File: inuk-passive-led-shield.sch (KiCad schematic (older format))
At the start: 12 parts, among them J1 Conn_01x04_Male, J2 Conn_01x10_Male, J3 Conn_01x02_Male

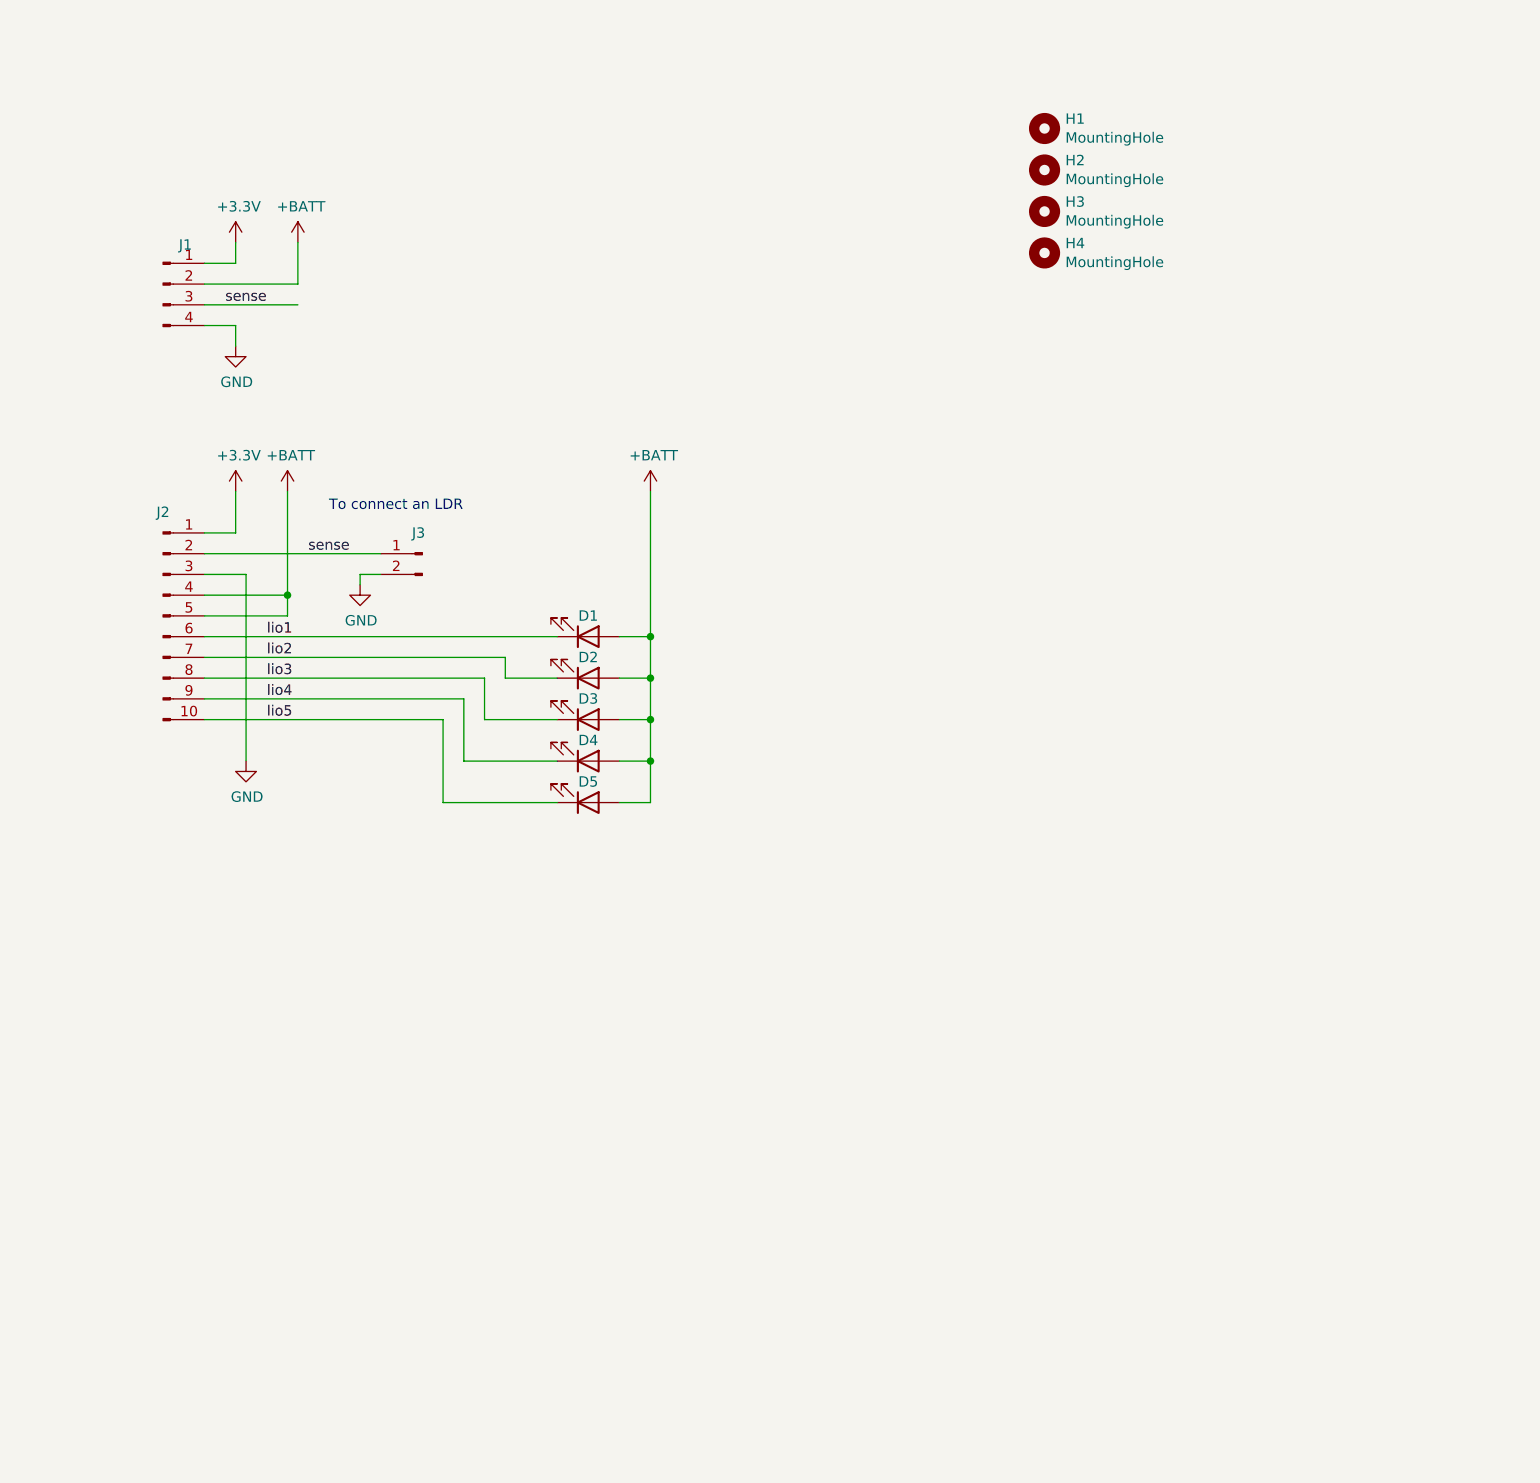
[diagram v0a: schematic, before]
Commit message: added logo and info text for rev 0.9
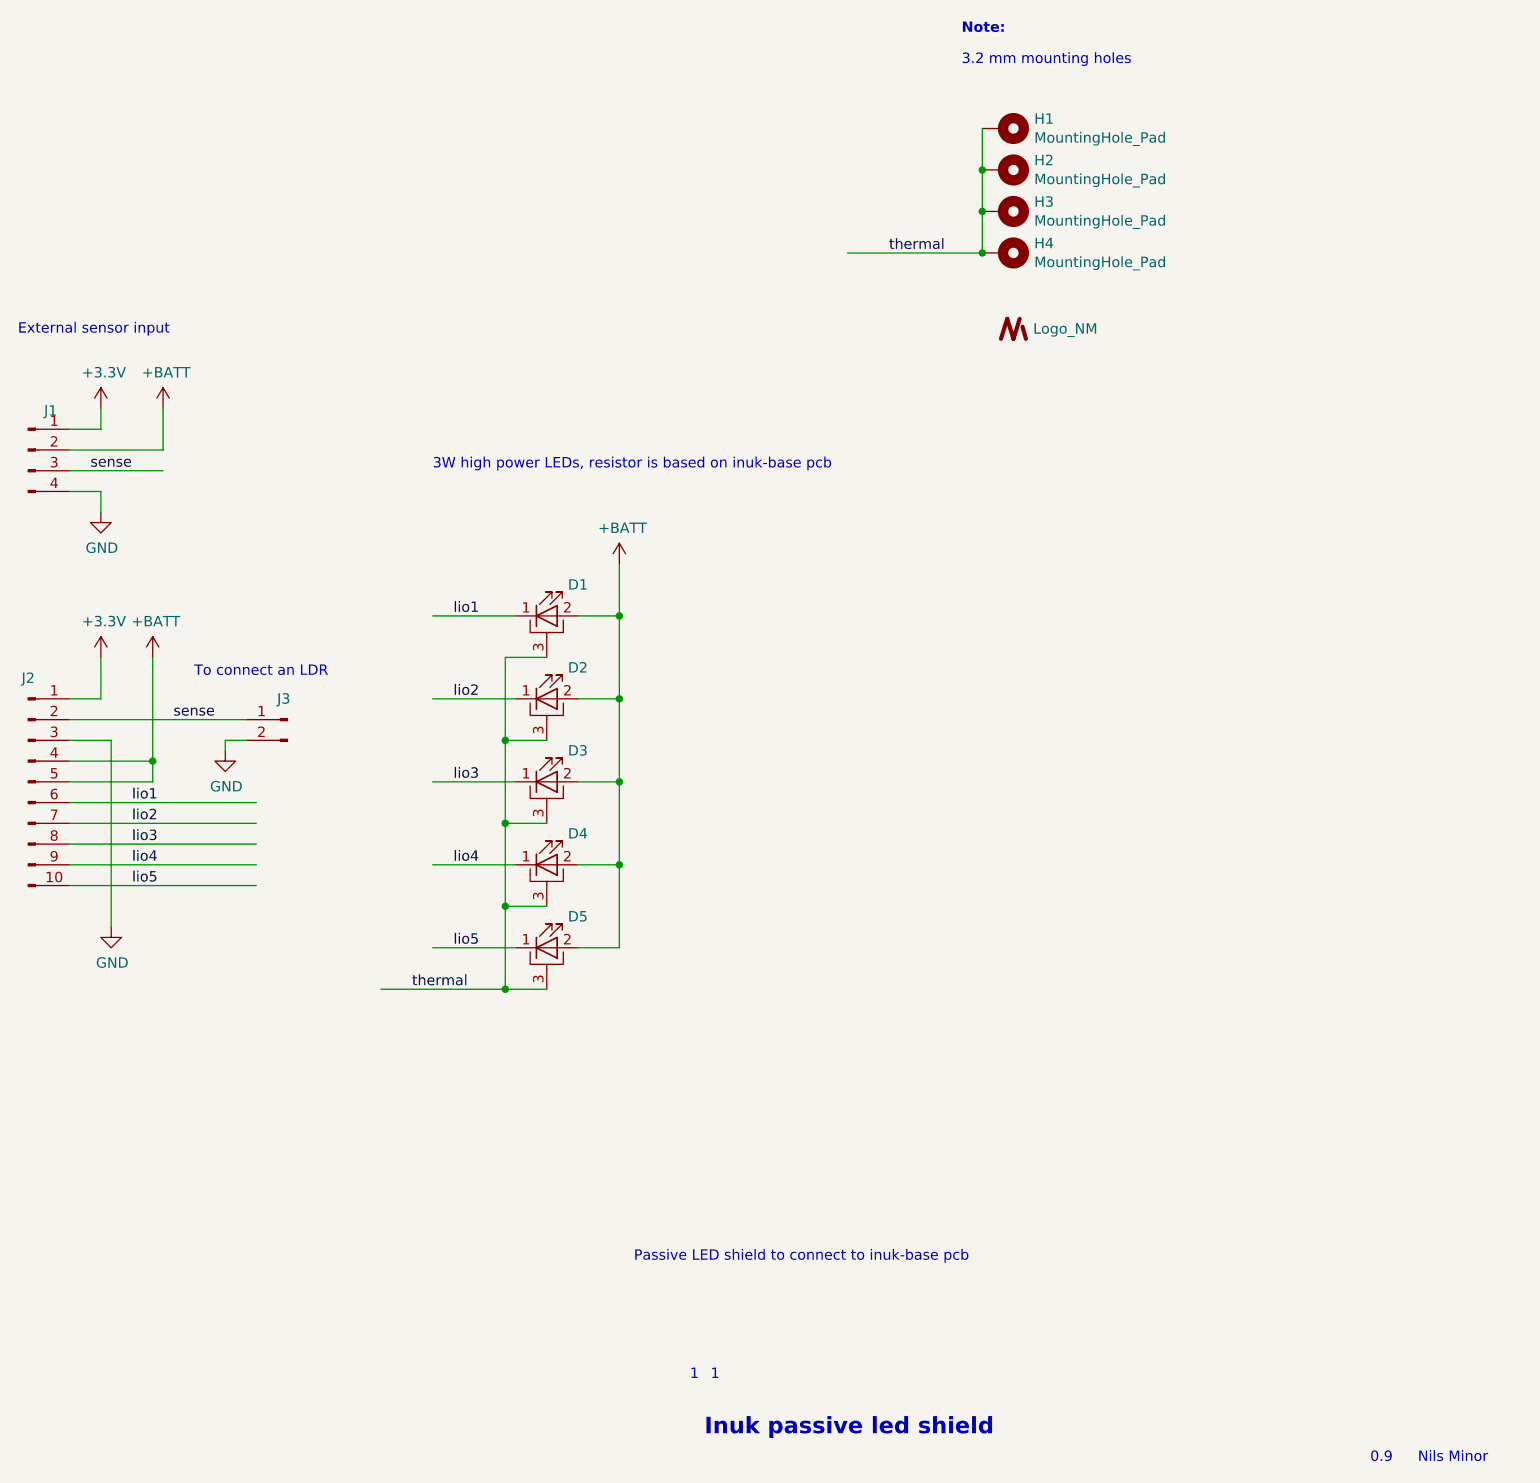
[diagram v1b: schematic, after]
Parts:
- removed D1, D2, D3, D4, D5: LED, LED_SMD:LED_1W_3W_R8, symbol Device:LED
- removed H1, H2, H3, H4: MountingHole, MountingHole:MountingHole_3.2mm_M3_Pad_Via, symbol Mechanical:MountingHole
- added D1, D2, D3, D4, D5: LED_PAD, LED_SMD:LED_1W_3W_R8, symbol Device:LED_PAD
- added H1, H2, H3, H4: MountingHole_Pad, MountingHole:MountingHole_3.2mm_M3_Pad_Via, symbol Mechanical:MountingHole_Pad
- added U1: Logo_NM, Custom:Logo_NM, symbol Custom:Logo_NM
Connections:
- net labels added: thermal
- wire segments 41 -> 52
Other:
- note added: "0.9"
- note added: "1"
- note added: "3.2 mm mounting holes"
- note added: "3W high power LEDs, resistor is based on inuk-base pcb"
- note added: "External sensor input\n"
- note added: "Inuk passive led shield"
- note added: "Nils Minor"
- note added: "Note:"
- note added: "Passive LED shield to connect to inuk-base pcb"
- moved on the sheet: J1, J2, J3

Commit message: resized board to 27 x 100 to fit on 100x100 panel
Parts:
- J1: MPN (none) -> 61300411121
- J2: MPN (none) -> 61301011121
- J3: MPN (none) -> 61300211121
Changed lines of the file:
@@
 F 2 "Connector_PinHeader_2.54mm:PinHeader_1x10_P2.54mm_Horizontal" H 4100 4350 50  0001 C CNN
 F 3 "~" H 4100 4350 50  0001 C CNN
+F 4 "61301011121" H 4100 4350 50  0001 C CNN "MPN"
 	1    4100 4350
 	1    0    0    -1
@@
 F 2 "Connector_PinHeader_2.54mm:PinHeader_1x02_P2.54mm_Vertical" H 5350 4050 50  0001 C CNN
 F 3 "~" H 5350 4050 50  0001 C CNN
+F 4 "61300211121" H 5350 4050 50  0001 C CNN "MPN"
 	1    5350 4050
 	-1   0    0    -1
 $EndComp
-$Comp
-L power:GND #PWR0105
-U 1 1 5EAF031C
-P 5050 4200
-F 0 "#PWR0105" H 5050 3950 50  0001 C CNN
-F 1 "GND" H 5055 4027 50  0000 C CNN
-F 2 "" H 5050 4200 50  0001 C CNN
-F 3 "" H 5050 4200 50  0001 C CNN
-	1    5050 4200
-	1    0    0    -1
-$EndComp
-Wire Wire Line
-	5150 4150 5050 4150
-Wire Wire Line
-	5050 4150 5050 4200
-Text Notes 4900 3850 0    50   ~ 0
+Text Notes 4850 4300 0    50   ~ 0
 To connect an LDR\n
 Text Label 4600 4450 0    50   ~ 0
@@
 F 2 "Connector_PinHeader_2.54mm:PinHeader_1x04_P2.54mm_Vertical" H 4100 2750 50  0001 C CNN
 F 3 "~" H 4100 2750 50  0001 C CNN
+F 4 "61300411121" H 4100 2750 50  0001 C CNN "MPN"
 	1    4100 2750
 	1    0    0    -1
@@
 Text Notes 7020 6670 0    50   ~ 0
 Passive LED shield to connect to inuk-base pcb
+$Comp
+L power:+3.3V #PWR?
+U 1 1 5E98C1A2
+P 5100 3750
+F 0 "#PWR?" H 5100 3600 50  0001 C CNN
+F 1 "+3.3V" H 5115 3923 50  0000 C CNN
+F 2 "" H 5100 3750 50  0001 C CNN
+F 3 "" H 5100 3750 50  0001 C CNN
+	1    5100 3750
+	1    0    0    -1
+$EndComp
+Wire Wire Line
+	5150 4150 5100 4150
+Wire Wire Line
+	5100 4150 5100 3750
 $EndSCHEMATC

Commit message: created production files
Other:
- note added: "1.0"
- note removed: "0.9"
- note removed: "1"
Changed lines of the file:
@@
 L Custom:Logo_NM U1
 U 1 1 5EB6FA5B
-P 8850 2200
-F 0 "U1" H 8750 2250 50  0001 C CNN
-F 1 "Logo_NM" H 8945 2234 50  0000 L CNN
-F 2 "Custom:Logo_NM" H 8894 2130 50  0001 C CNN
-F 3 "" H 8790 2186 50  0001 C CNN
-	1    8850 2200
+P 8150 1250
+F 0 "U1" H 8050 1300 50  0001 C CNN
+F 1 "Logo_NM" H 8245 1284 50  0000 L CNN
+F 2 "Custom:Logo_NM" H 8194 1180 50  0001 C CNN
+F 3 "" H 8090 1236 50  0001 C CNN
+	1    8150 1250
 	1    0    0    -1
 $EndComp
@@
 Text Notes 6050 2850 0    50   ~ 0
 3W high power LEDs, resistor is based on inuk-base pcb
-Text Notes 7390 7240 0    50   ~ 0
-1
-Text Notes 7290 7240 0    50   ~ 0
-1
 Text Notes 7360 7510 0    79   ~ 16
 Inuk passive led shield
 Text Notes 10570 7640 0    50   ~ 0
-0.9
+1.0
 Text Notes 10800 7640 0    50   ~ 0
 Nils Minor
